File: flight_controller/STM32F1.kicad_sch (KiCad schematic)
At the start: 21 parts, among them SW3 6.0*6.0*6.0, U12 HB-PH9-12727PB2GOB, U2 STM32F103C8T6, X3 TAXM8M4RDBCCT2T

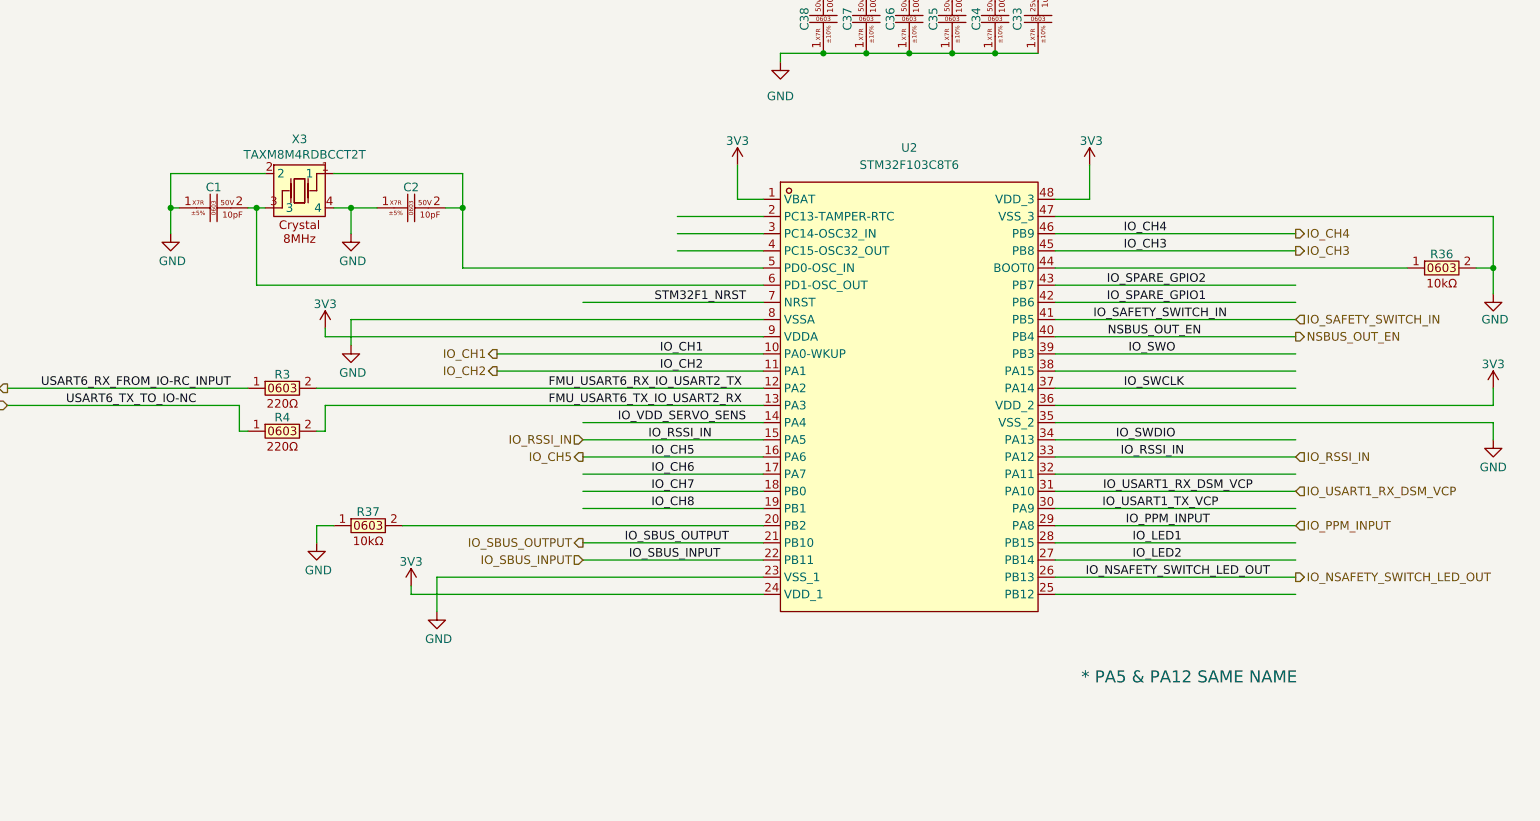
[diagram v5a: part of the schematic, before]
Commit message: Schematic complete, ready for layout. Added USB, TPs, power conn, updated clocks, ran Rules Checker and general review
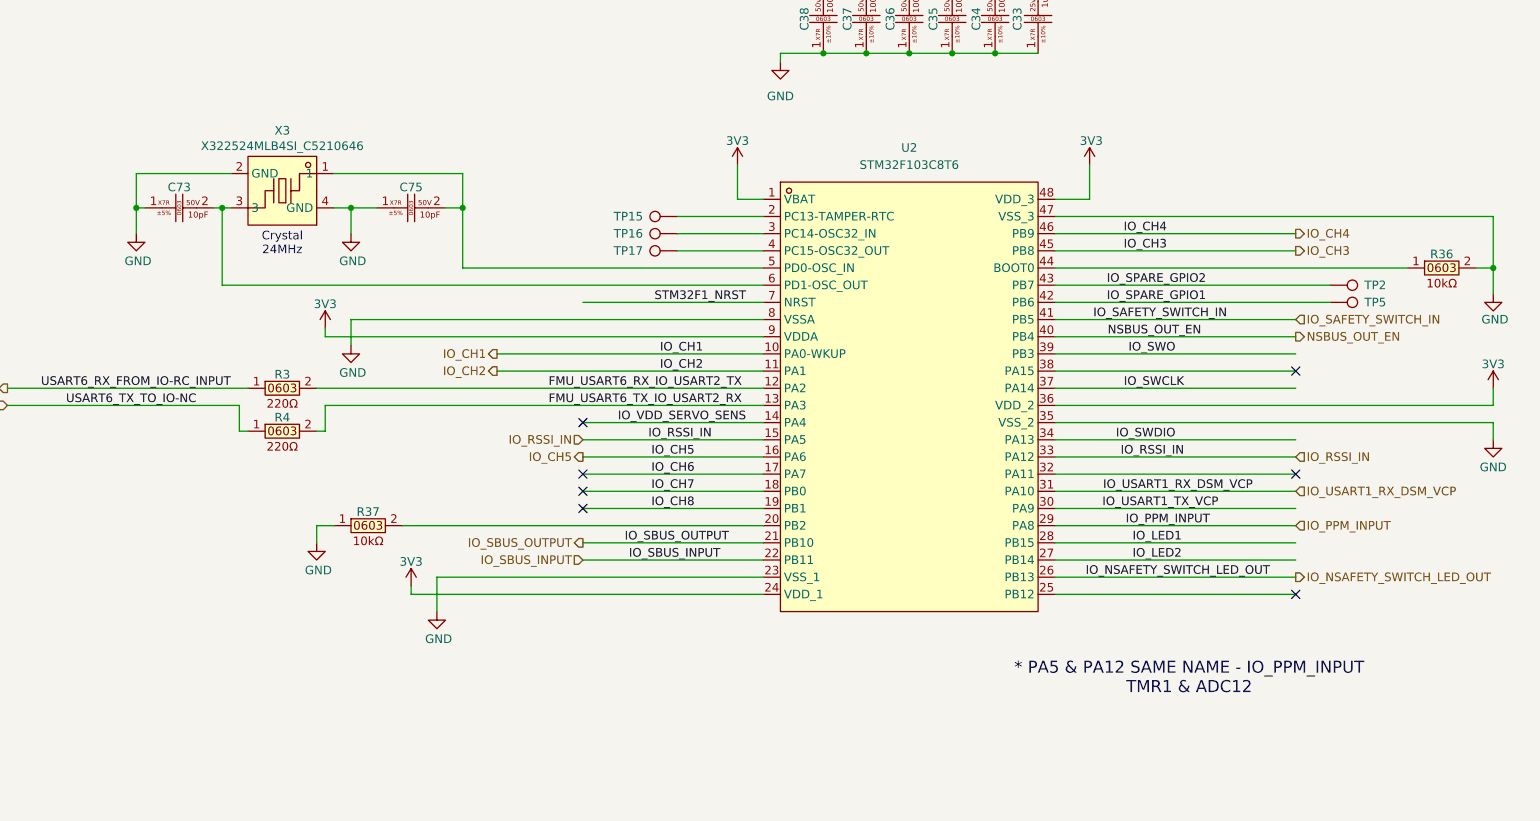
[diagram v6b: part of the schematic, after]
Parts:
- removed C1, C2: CC0603JRNPO9BN100 (10pF , 0603 ,50V ,X7R), easyeda2kicad:C0603, symbol lampelKicadLIB:CC0603JRNPO9BN100 (10pF , 0603 ,50V ,X7R)
- removed X3: TAXM8M4RDBCCT2T, easyeda2kicad:CRYSTAL-SMD_4P-L3.2-W2.5-BL, symbol lampelKicadLIB:TAXM8M4RDBCCT2T
- added C73, C75: CC0603JRNPO9BN100 (10pF , 0603 ,50V ,X7R), easyeda2kicad:C0603, symbol lampelKicadLIB:CC0603JRNPO9BN100 (10pF , 0603 ,50V ,X7R)
- added TP15, TP16, TP17, TP2, TP5: TestPoint, TestPoint:TestPoint_Pad_2.0x2.0mm, symbol Connector:TestPoint
- added X3: X322524MLB4SI_C5210646, easyeda2kicad:CRYSTAL-SMD_4P-L3.2-W2.5-BL, symbol lampelKicadLIB:X322524MLB4SI_C5210646
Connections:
- net GND: now also C73.1, C75.1, X3.2 (GND), X3.4 (GND)
- net IO_SPARE_GPIO1: now also TP5.1
- net IO_SPARE_GPIO2: now also TP2.1
- net at U2.5 (PD0-OSC_IN): now also C75.2, X3.1
- net at U2.2 (PC13-TAMPER-RTC): now also TP15.1
- net at U2.3 (PC14-OSC32_IN): now also TP16.1
- net at U2.4 (PC15-OSC32_OUT): now also TP17.1
- net at U2.6 (PD1-OSC_OUT): now also C73.2, X3.3
- no-connect marks 5 -> 12
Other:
- note added: "* PA5 & PA12 SAME NAME - IO_PPM_INPUT TMR1 & ADC12"
- note added: "Crystal 24MHz"
- note removed: "* PA5 & PA12 SAME NAME"

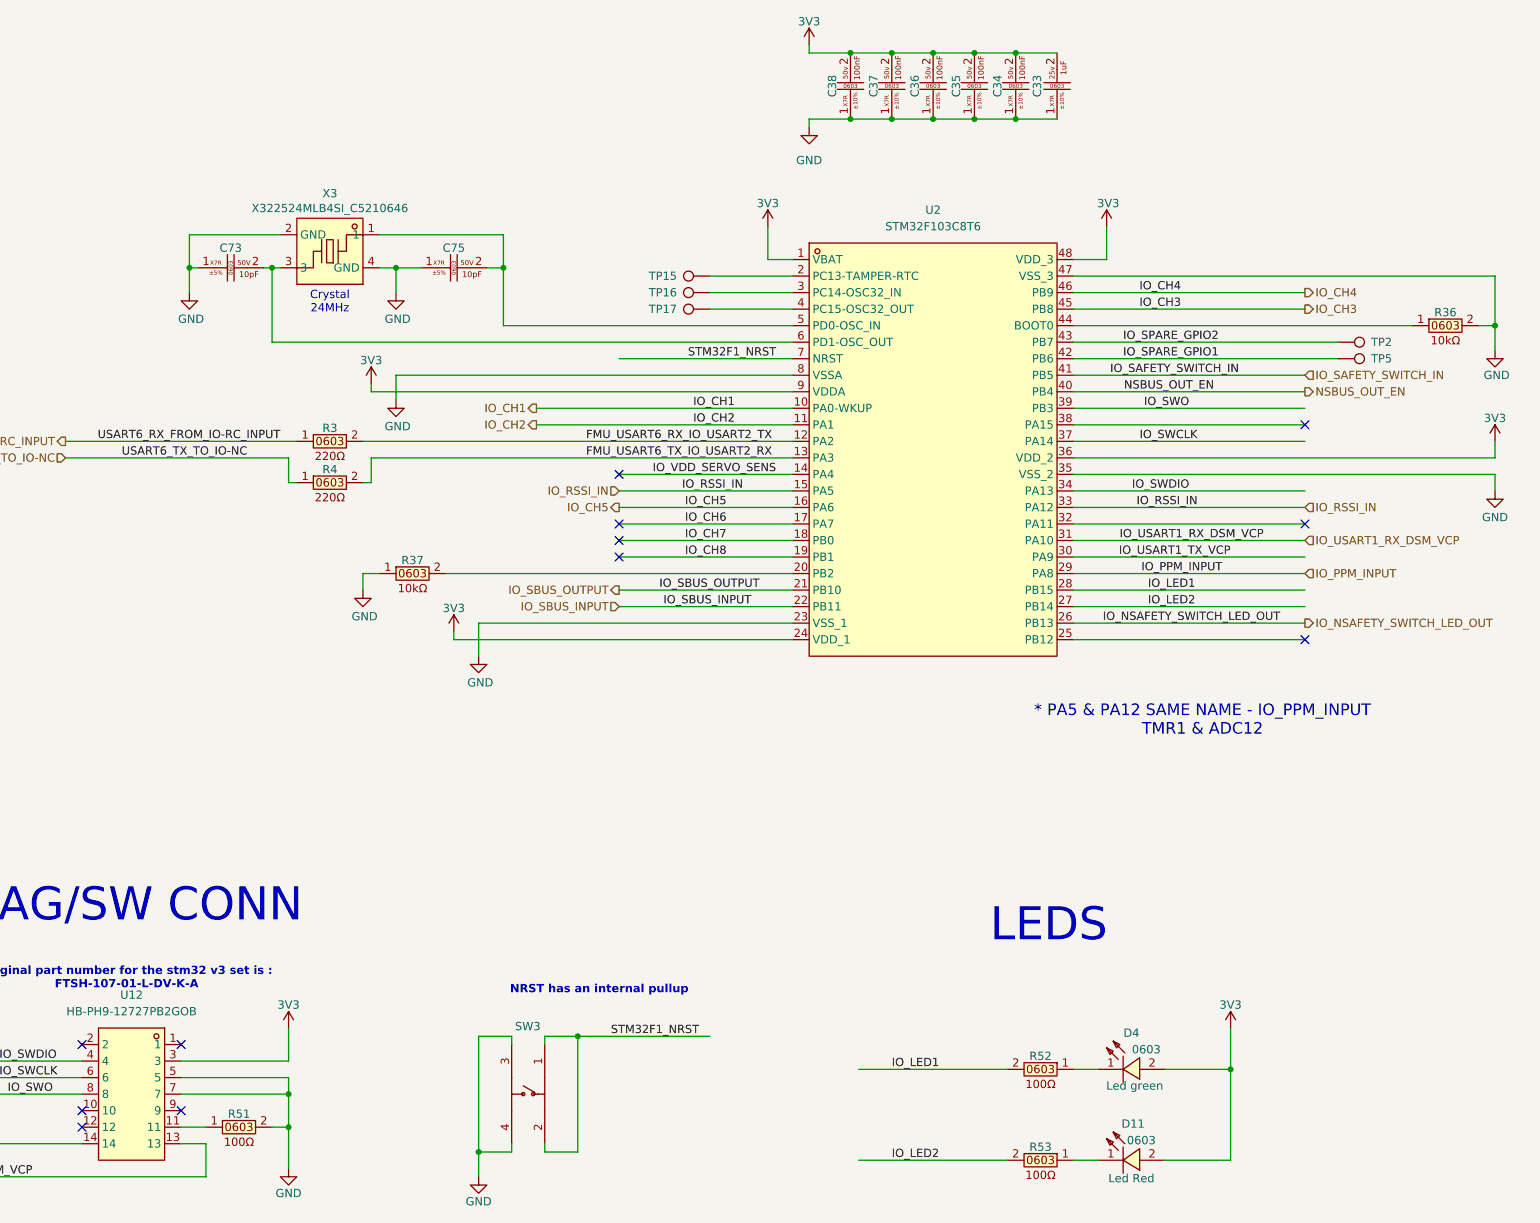
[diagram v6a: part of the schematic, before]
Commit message: Started the placement process
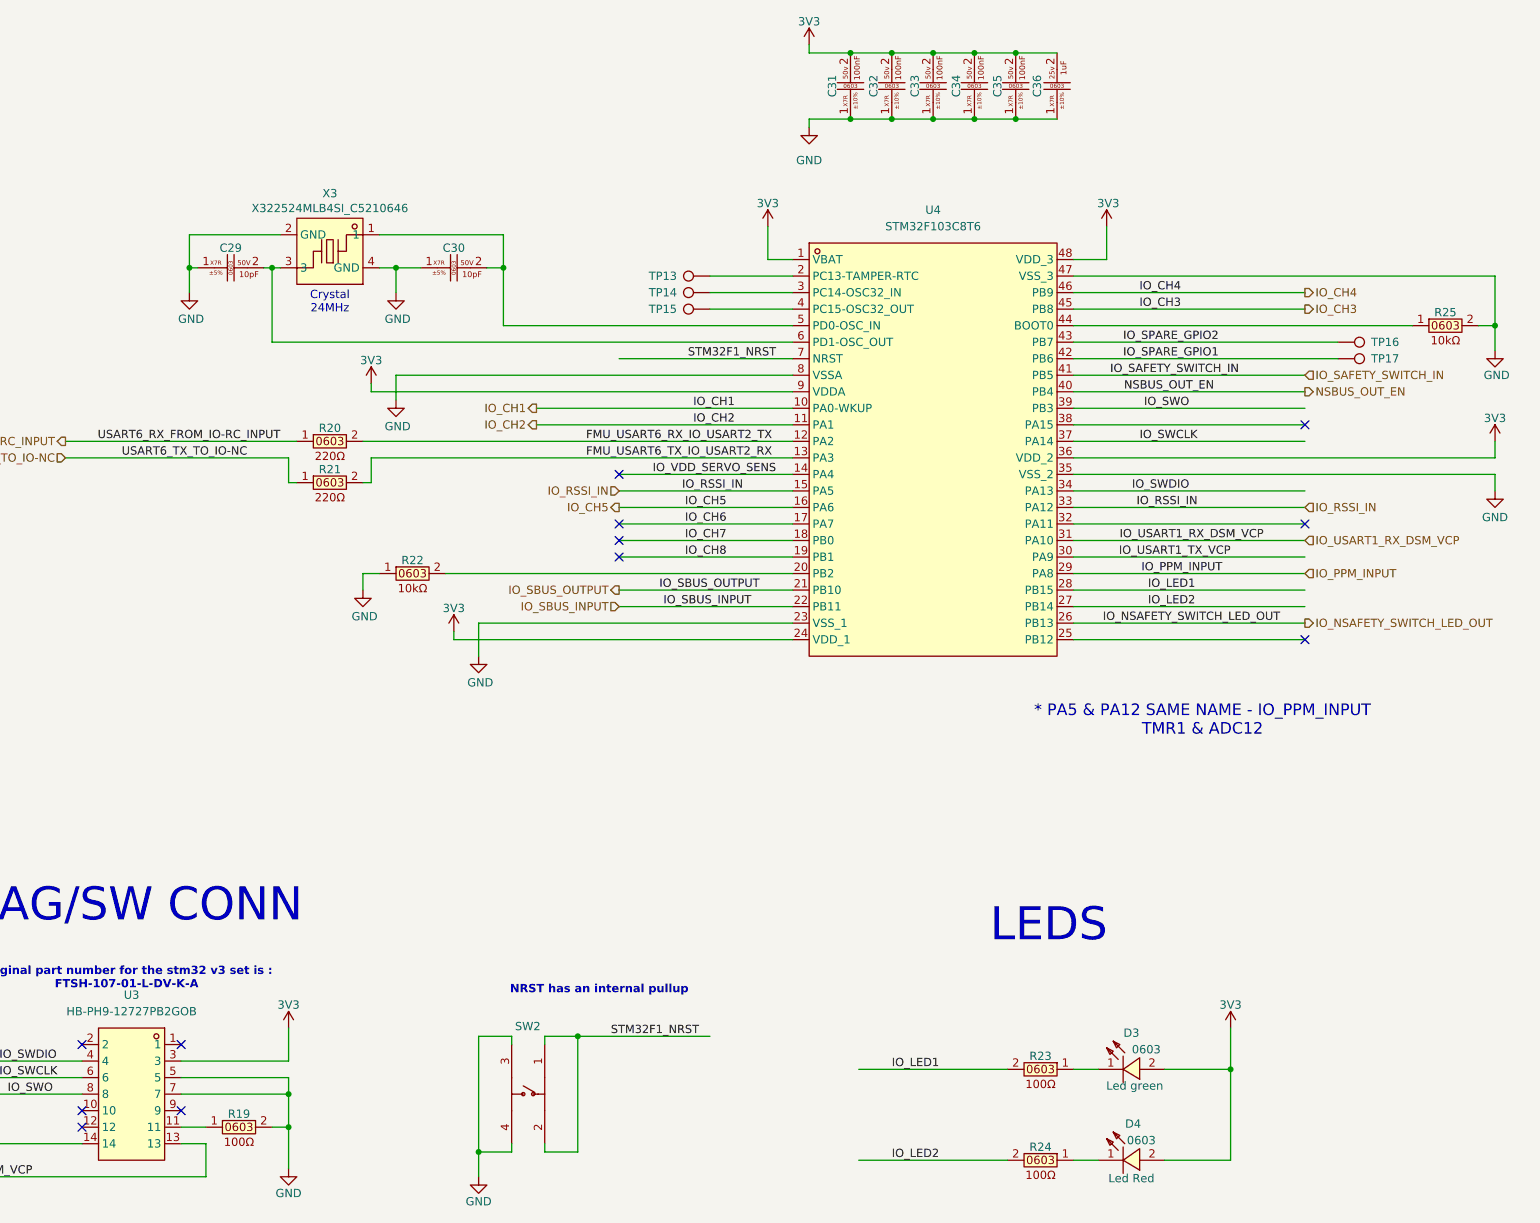
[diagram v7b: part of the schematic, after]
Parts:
- renumbered C73 to C29, C75 to C30, C38 to C31, C37 to C32, C36 to C33, C35 to C34, C34 to C35, C33 to C36, D4 to D3, D11 to D4, R51 to R19, R3 to R20, R4 to R21, R37 to R22, R52 to R23, R53 to R24, R36 to R25, SW3 to SW2, TP15 to TP13, TP16 to TP14, TP17 to TP15, TP2 to TP16, TP5 to TP17, U12 to U3, U2 to U4

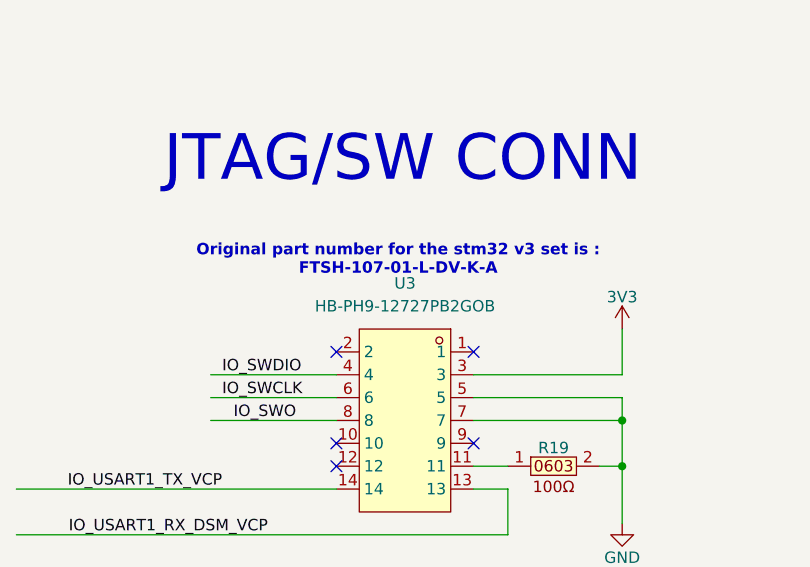
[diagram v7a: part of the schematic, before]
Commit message: renamed some connectors to j instead of cn
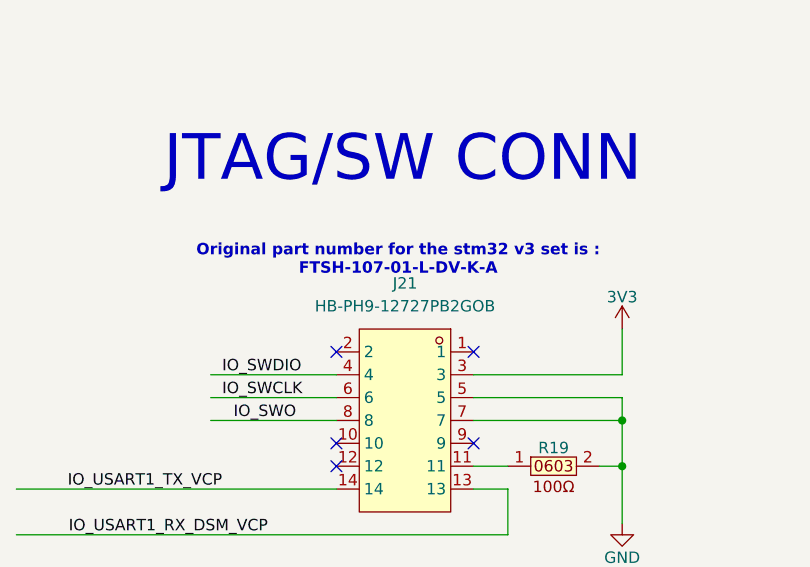
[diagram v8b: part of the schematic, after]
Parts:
- renumbered U3 to J21
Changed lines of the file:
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@@
 		(on_board yes)
 		(dnp no)
-		(property "Reference" "U3"
+		(property "Reference" "J21"
 			(at 231.14 234.95 0)
 			(effects
@@
 			(project "FP_BOARD"
 				(path "/17737359-1a8e-4237-8899-d9604030bc1d/e4f0bf63-f781-4c4e-9f6b-c9f89551cbca"
-					(reference "U3")
+					(reference "J21")
 					(unit 1)
 				)
